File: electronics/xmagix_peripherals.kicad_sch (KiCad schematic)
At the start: 16 parts, among them J1 Conn_02x05_Counter_Clockwise, J2 Conn_02x05_Counter_Clockwise, J3 Conn_01x02, SW1 SW_SPDT, SW2 SW_SPDT, U1 LT1009CZ, U2 TLV5618A, U5 MCP3202, U7 LM4040DIZ-5.0

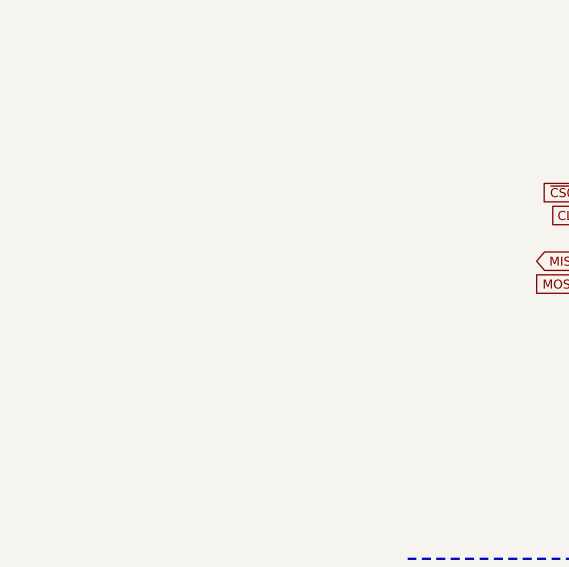
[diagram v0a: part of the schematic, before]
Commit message: schematics renamed, raspi4b gpio sch added
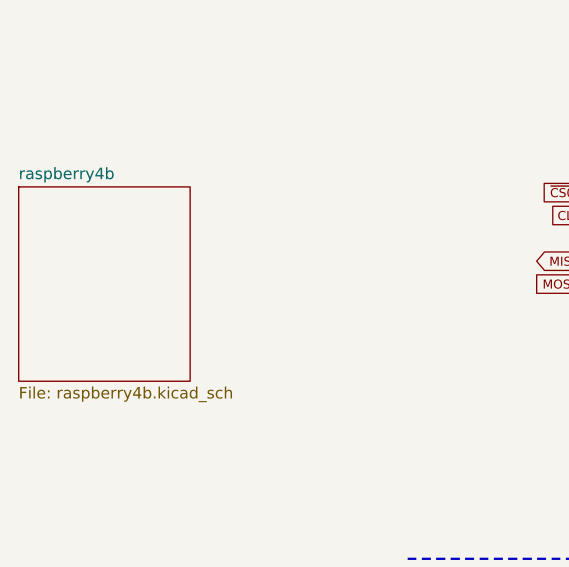
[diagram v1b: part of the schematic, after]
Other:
- added sheet raspberry4b (raspberry4b.kicad_sch)
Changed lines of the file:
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@@
     (company "RheinMain University of Applied Sciences")
     (comment 1 "by Dennis Hunter")
-    (comment 2 "!!WIP!!")
   )
   (junction (at 207.01 45.72) (diameter 0) (color 0 0 0 0)
@@
     (pin "3")
     (instances
-      (project "raspberry"
+      (project "xmagix_peripherals"
         (path "/38b26eea-f38c-484f-9bac-db518f332ae0"
           (reference "U1") (unit 1)
@@
     (pin "3")
     (instances
-      (project "raspberry"
+      (project "xmagix_peripherals"
         (path "/38b26eea-f38c-484f-9bac-db518f332ae0"
           (reference "SW1") (unit 1)
@@
     (pin "1")
     (instances
-      (project "raspberry"
+      (project "xmagix_peripherals"
         (path "/38b26eea-f38c-484f-9bac-db518f332ae0"
           (reference "#PWR05") (unit 1)
@@
     (pin "2")
     (instances
-      (project "raspberry"
+      (project "xmagix_peripherals"
         (path "/38b26eea-f38c-484f-9bac-db518f332ae0"
           (reference "J3") (unit 1)
@@
     (pin "1")
     (instances
-      (project "raspberry"
+      (project "xmagix_peripherals"
         (path "/38b26eea-f38c-484f-9bac-db518f332ae0"
           (reference "#PWR012") (unit 1)
@@
     (pin "9")
     (instances
-      (project "raspberry"
+      (project "xmagix_peripherals"
         (path "/38b26eea-f38c-484f-9bac-db518f332ae0"
           (reference "J2") (unit 1)
@@
     (pin "3")
     (instances
-      (project "raspberry"
+      (project "xmagix_peripherals"
         (path "/38b26eea-f38c-484f-9bac-db518f332ae0"
           (reference "SW2") (unit 1)
@@
     (pin "1")
     (instances
-      (project "raspberry"
+      (project "xmagix_peripherals"
         (path "/38b26eea-f38c-484f-9bac-db518f332ae0"
           (reference "#PWR013") (unit 1)
@@
     (pin "2")
     (instances
-      (project "raspberry"
+      (project "xmagix_peripherals"
         (path "/38b26eea-f38c-484f-9bac-db518f332ae0"
           (reference "C2") (unit 1)
@@
     (pin "8")
     (instances
-      (project "raspberry"
+      (project "xmagix_peripherals"
         (path "/38b26eea-f38c-484f-9bac-db518f332ae0"
           (reference "U2") (unit 1)
@@
     (pin "1")
     (instances
-      (project "raspberry"
+      (project "xmagix_peripherals"
         (path "/38b26eea-f38c-484f-9bac-db518f332ae0"
           (reference "#PWR022") (unit 1)
@@
     (pin "1")
     (instances
-      (project "raspberry"
+      (project "xmagix_peripherals"
         (path "/38b26eea-f38c-484f-9bac-db518f332ae0"
           (reference "#PWR07") (unit 1)
@@
     (pin "1")
     (instances
-      (project "raspberry"
+      (project "xmagix_peripherals"
         (path "/38b26eea-f38c-484f-9bac-db518f332ae0"
           (reference "#PWR06") (unit 1)
@@
     (pin "1")
     (instances
-      (project "raspberry"
+      (project "xmagix_peripherals"
         (path "/38b26eea-f38c-484f-9bac-db518f332ae0"
           (reference "#PWR019") (unit 1)
@@
     (pin "1")
     (instances
-      (project "raspberry"
+      (project "xmagix_peripherals"
         (path "/38b26eea-f38c-484f-9bac-db518f332ae0"
           (reference "#PWR023") (unit 1)
@@
     (pin "1")
     (instances
-      (project "raspberry"
+      (project "xmagix_peripherals"
         (path "/38b26eea-f38c-484f-9bac-db518f332ae0"
           (reference "#PWR025") (unit 1)
@@
     (pin "2")
     (instances
-      (project "raspberry"
+      (project "xmagix_peripherals"
         (path "/38b26eea-f38c-484f-9bac-db518f332ae0"
           (reference "C1") (unit 1)
@@
     (pin "1")
     (instances
-      (project "raspberry"
+      (project "xmagix_peripherals"
         (path "/38b26eea-f38c-484f-9bac-db518f332ae0"
           (reference "#PWR017") (unit 1)
@@
     (pin "1")
     (instances
-      (project "raspberry"
+      (project "xmagix_peripherals"
         (path "/38b26eea-f38c-484f-9bac-db518f332ae0"
           (reference "#PWR020") (unit 1)
@@
     (pin "1")
     (instances
-      (project "raspberry"
+      (project "xmagix_peripherals"
         (path "/38b26eea-f38c-484f-9bac-db518f332ae0"
           (reference "#PWR021") (unit 1)
@@
     (pin "1")
     (instances
-      (project "raspberry"
+      (project "xmagix_peripherals"
         (path "/38b26eea-f38c-484f-9bac-db518f332ae0"
           (reference "#PWR011") (unit 1)
@@
     (pin "1")
     (instances
-      (project "raspberry"
+      (project "xmagix_peripherals"
         (path "/38b26eea-f38c-484f-9bac-db518f332ae0"
           (reference "#PWR015") (unit 1)
@@
     (pin "2")
     (instances
-      (project "raspberry"
+      (project "xmagix_peripherals"
         (path "/38b26eea-f38c-484f-9bac-db518f332ae0"
           (reference "R1") (unit 1)
@@
     (pin "9")
     (instances
-      (project "raspberry"
+      (project "xmagix_peripherals"
         (path "/38b26eea-f38c-484f-9bac-db518f332ae0"
           (reference "J1") (unit 1)
@@
     (pin "1")
     (instances
-      (project "raspberry"
+      (project "xmagix_peripherals"
         (path "/38b26eea-f38c-484f-9bac-db518f332ae0"
           (reference "#PWR014") (unit 1)
@@
     (pin "1")
     (instances
-      (project "raspberry"
+      (project "xmagix_peripherals"
         (path "/38b26eea-f38c-484f-9bac-db518f332ae0"
           (reference "#PWR08") (unit 1)
@@
     (pin "1")
     (instances
-      (project "raspberry"
+      (project "xmagix_peripherals"
         (path "/38b26eea-f38c-484f-9bac-db518f332ae0"
           (reference "#PWR016") (unit 1)
@@
     (pin "1")
     (instances
-      (project "raspberry"
+      (project "xmagix_peripherals"
         (path "/38b26eea-f38c-484f-9bac-db518f332ae0"
           (reference "#PWR018") (unit 1)
@@
     (pin "2")
     (instances
-      (project "raspberry"
+      (project "xmagix_peripherals"
         (path "/38b26eea-f38c-484f-9bac-db518f332ae0"
           (reference "R4") (unit 1)
@@
     (pin "1")
     (instances
-      (project "raspberry"
+      (project "xmagix_peripherals"
         (path "/38b26eea-f38c-484f-9bac-db518f332ae0"
           (reference "#PWR024") (unit 1)
@@
     (pin "8")
     (instances
-      (project "raspberry"
+      (project "xmagix_peripherals"
         (path "/38b26eea-f38c-484f-9bac-db518f332ae0"
           (reference "U5") (unit 1)
@@
     (pin "2")
     (instances
-      (project "raspberry"
+      (project "xmagix_peripherals"
         (path "/38b26eea-f38c-484f-9bac-db518f332ae0"
           (reference "R5") (unit 1)
@@
     (pin "1")
     (instances
-      (project "raspberry"
+      (project "xmagix_peripherals"
         (path "/38b26eea-f38c-484f-9bac-db518f332ae0"
           (reference "#PWR01") (unit 1)
@@
     (pin "1")
     (instances
-      (project "raspberry"
+      (project "xmagix_peripherals"
         (path "/38b26eea-f38c-484f-9bac-db518f332ae0"
           (reference "#PWR0101") (unit 1)
@@
     (pin "1")
     (instances
-      (project "raspberry"
+      (project "xmagix_peripherals"
         (path "/38b26eea-f38c-484f-9bac-db518f332ae0"
           (reference "#PWR04") (unit 1)
@@
     (pin "1")
     (instances
-      (project "raspberry"
+      (project "xmagix_peripherals"
         (path "/38b26eea-f38c-484f-9bac-db518f332ae0"
           (reference "#PWR026") (unit 1)
@@
     (pin "2")
     (instances
-      (project "raspberry"
+      (project "xmagix_peripherals"
         (path "/38b26eea-f38c-484f-9bac-db518f332ae0"
           (reference "R2") (unit 1)
@@
     (pin "3")
     (instances
-      (project "raspberry"
+      (project "xmagix_peripherals"
         (path "/38b26eea-f38c-484f-9bac-db518f332ae0"
           (reference "U7") (unit 1)
@@
     (pin "2")
     (instances
-      (project "raspberry"
+      (project "xmagix_peripherals"
         (path "/38b26eea-f38c-484f-9bac-db518f332ae0"
           (reference "R3") (unit 1)
@@
     (pin "1")
     (instances
-      (project "raspberry"
+      (project "xmagix_peripherals"
         (path "/38b26eea-f38c-484f-9bac-db518f332ae0"
           (reference "#PWR03") (unit 1)
@@
     (pin "1")
     (instances
-      (project "raspberry"
+      (project "xmagix_peripherals"
         (path "/38b26eea-f38c-484f-9bac-db518f332ae0"
           (reference "#PWR02") (unit 1)
@@
       )
     )
+  )
+  (sheet (at -31.115 66.675) (size 19.05 21.59) (fields_autoplaced)
+    (stroke (width 0.1524) (type solid))
+    (fill (color 0 0 0 0.0000))
+    (property "Sheetname" "raspberry4b" (at -31.115 65.9634 0)
+      (effects (font (size 1.27 1.27)) (justify left bottom))
+    )
+    (property "Sheetfile" "raspberry4b.kicad_sch" (at -31.115 88.8496 0)
+      (effects (font (size 1.27 1.27)) (justify left top))
+    )
+    (instances
+      (project "xmagix_peripherals"
+        (path "/38b26eea-f38c-484f-9bac-db518f332ae0" (page "2"))
+      )
+    )

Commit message: section kinematics
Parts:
- R2, R3: value 470R -> ~; footprint (none) -> Resistor_THT:R_Axial_DIN0204_L3.6mm_D1.6mm_P7.62mm_Horizontal
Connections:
- net +3.3V: now also R2.2, R3.2
- net +5V: no longer R2.2, R3.2
- net Endstop Det: now also R3.1
- net Endstop Smpl: now also R2.1
- net GND: now also SW1.2 (B), SW2.2 (B)
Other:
- note added: "Internal Pull-Up"
- moved on the sheet: SW1, SW2
